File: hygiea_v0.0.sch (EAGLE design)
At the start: 45 parts, among them U1 3.3V/150mA, U2 BNO055, U3 CRYSTAL_8X3.8SMD

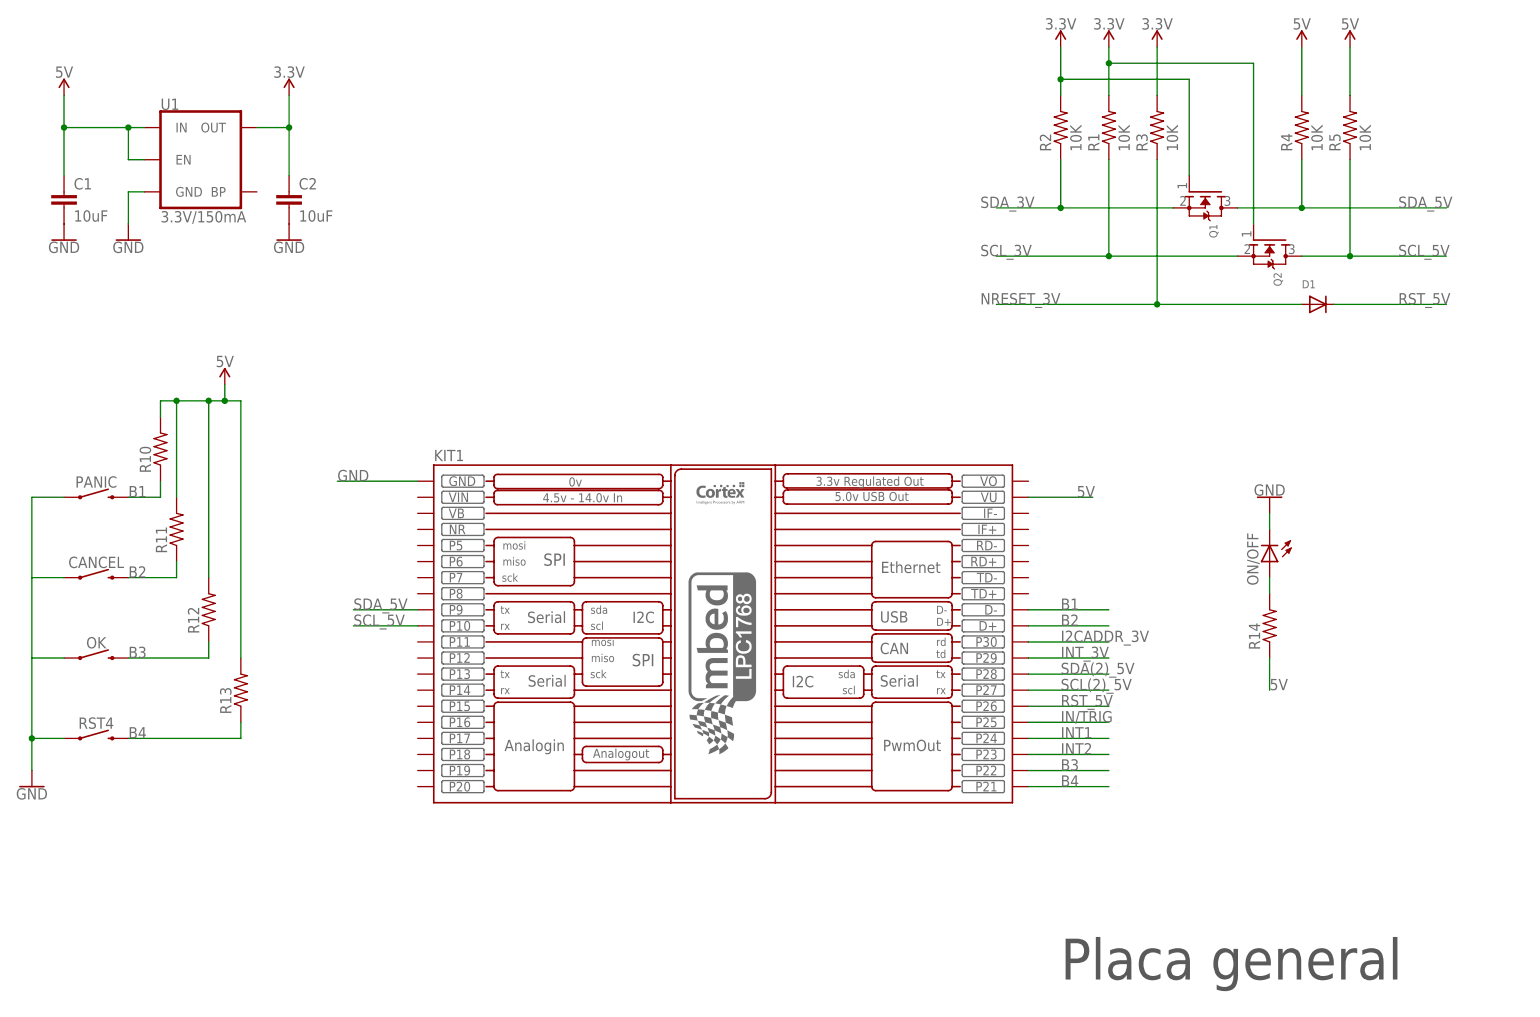
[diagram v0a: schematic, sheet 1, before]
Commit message: Version barata, push buttons standar
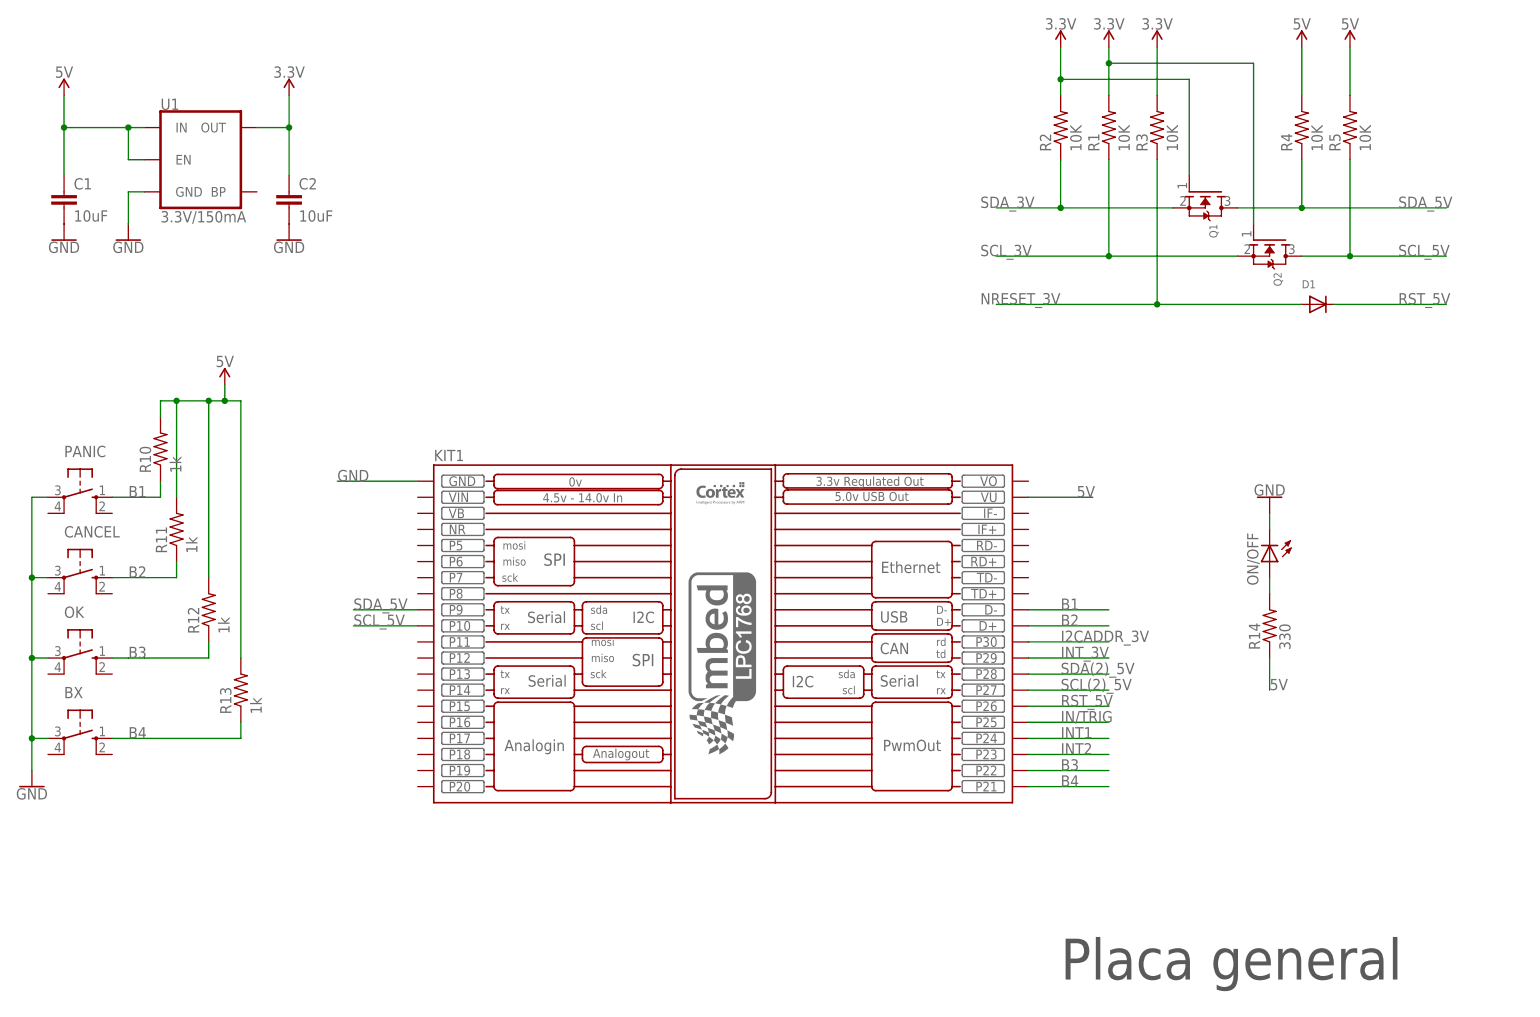
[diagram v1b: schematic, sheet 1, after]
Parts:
- removed RST4: MOMENTARY-SWITCH-SPST-SMD-5.2-REDUNDANT, SparkFun-Switches:MOMENTARY-SWITCH-SPST-SMD-5.2-REDUNDANT
- added BX: (no value), switch-omron:10-XX
- CANCEL, OK, PANIC, RST: value MOMENTARY-SWITCH-SPST-SMD-5.2-REDUNDANT -> (none); device SparkFun-Switches:MOMENTARY-SWITCH-SPST-SMD-5.2-REDUNDANT -> switch-omron:10-XX
- R10, R11, R12, R13: value (none) -> 1k
- R14: value (none) -> 330
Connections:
- net AT_RESET: now also RST.S; no longer RST.2
- net B1: now also PANIC.S; no longer PANIC.2
- net B2: now also CANCEL.S; no longer CANCEL.2
- net B3: now also OK.S; no longer OK.2
- net B4: now also BX.S; no longer RST4.2
- net GND: now also BX.P, CANCEL.P, OK.P, PANIC.P, RST.P; no longer CANCEL.1, OK.1, PANIC.1, RST.1, RST4.1
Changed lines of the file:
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@@
 <part name="GND19" library="SparkFun-PowerSymbols" deviceset="GND" device=""/>
 <part name="BLE/ICSP" library="adafruit" deviceset="PINHD-1X10" device=""/>
-<part name="RST" library="SparkFun-Switches" deviceset="MOMENTARY-SWITCH-SPST" device="-SMD-5.2-REDUNDANT" value=""/>
 <part name="R7" library="adafruit" deviceset="R-US_" device="R0805" value="1k"/>
 <part name="R8" library="adafruit" deviceset="R-US_" device="R0805" value="10k"/>
@@
 <part name="SUPPLY14" library="SparkFun-PowerSymbols" deviceset="5V" device=""/>
 <part name="JP1" library="jumper" library_urn="urn:adsk.eagle:library:252" deviceset="JP2E" device="" package3d_urn="urn:adsk.eagle:package:15452/1"/>
-<part name="PANIC" library="SparkFun-Switches" deviceset="MOMENTARY-SWITCH-SPST" device="-SMD-5.2-REDUNDANT" value=""/>
-<part name="CANCEL" library="SparkFun-Switches" deviceset="MOMENTARY-SWITCH-SPST" device="-SMD-5.2-REDUNDANT" value=""/>
-<part name="OK" library="SparkFun-Switches" deviceset="MOMENTARY-SWITCH-SPST" device="-SMD-5.2-REDUNDANT" value=""/>
-<part name="RST4" library="SparkFun-Switches" deviceset="MOMENTARY-SWITCH-SPST" device="-SMD-5.2-REDUNDANT" value=""/>
-<part name="R10" library="adafruit" deviceset="R-US_" device="R0805"/>
-<part name="R11" library="adafruit" deviceset="R-US_" device="R0805"/>
-<part name="R12" library="adafruit" deviceset="R-US_" device="R0805"/>
-<part name="R13" library="adafruit" deviceset="R-US_" device="R0805"/>
+<part name="R10" library="adafruit" deviceset="R-US_" device="R0805" value="1k"/>
+<part name="R11" library="adafruit" deviceset="R-US_" device="R0805" value="1k"/>
+<part name="R12" library="adafruit" deviceset="R-US_" device="R0805" value="1k"/>
+<part name="R13" library="adafruit" deviceset="R-US_" device="R0805" value="1k"/>
 <part name="GND22" library="SparkFun-PowerSymbols" deviceset="GND" device=""/>
 <part name="SUPPLY18" library="SparkFun-PowerSymbols" deviceset="5V" device=""/>
 <part name="ON/OFF" library="adafruit" deviceset="LED" device="CHIP-LED0805"/>
-<part name="R14" library="adafruit" deviceset="R-US_" device="R0805"/>
+<part name="R14" library="adafruit" deviceset="R-US_" device="R0805" value="330"/>
 <part name="GND23" library="SparkFun-PowerSymbols" deviceset="GND" device=""/>
+<part name="PANIC" library="switch-omron" library_urn="urn:adsk.eagle:library:377" deviceset="10-XX" device="" package3d_urn="urn:adsk.eagle:package:27496/1"/>
+<part name="CANCEL" library="switch-omron" library_urn="urn:adsk.eagle:library:377" deviceset="10-XX" device="" package3d_urn="urn:adsk.eagle:package:27496/1"/>
+<part name="OK" library="switch-omron" library_urn="urn:adsk.eagle:library:377" deviceset="10-XX" device="" package3d_urn="urn:adsk.eagle:package:27496/1"/>
+<part name="BX" library="switch-omron" library_urn="urn:adsk.eagle:library:377" deviceset="10-XX" device="" package3d_urn="urn:adsk.eagle:package:27496/1"/>
+<part name="RST" library="switch-omron" library_urn="urn:adsk.eagle:library:377" deviceset="10-XX" device="" package3d_urn="urn:adsk.eagle:package:27496/1"/>
 </parts>
 <sheets>
@@
 <instance part="SUPPLY4" gate="G$1" x="213.36" y="172.72"/>
 <instance part="SUPPLY5" gate="G$1" x="220.98" y="172.72"/>
-<instance part="PANIC" gate="G$1" x="22.86" y="101.6"/>
-<instance part="CANCEL" gate="G$1" x="22.86" y="88.9"/>
-<instance part="OK" gate="G$1" x="22.86" y="76.2"/>
-<instance part="RST4" gate="G$1" x="22.86" y="63.5"/>
 <instance part="R10" gate="G$1" x="33.02" y="109.22" rot="R90"/>
 <instance part="R11" gate="G$1" x="35.56" y="96.52" rot="R90"/>
@@
 <instance part="R14" gate="G$1" x="208.28" y="81.28" rot="R90"/>
 <instance part="GND23" gate="1" x="208.28" y="101.6" rot="R180"/>
+<instance part="PANIC" gate="1" x="20.32" y="101.6" rot="R270"/>
+<instance part="CANCEL" gate="1" x="20.32" y="88.9" rot="R270"/>
+<instance part="OK" gate="1" x="20.32" y="76.2" rot="R270"/>
+<instance part="BX" gate="1" x="20.32" y="63.5" rot="R270"/>
 </instances>
 <busses>
@@
 </segment>
 <segment>
-<pinref part="RST4" gate="G$1" pin="1"/>
 <pinref part="GND22" gate="1" pin="GND"/>
-<wire x1="17.78" y1="63.5" x2="12.7" y2="63.5" width="0.1524" layer="91"/>
+<pinref part="PANIC" gate="1" pin="P"/>
+<wire x1="15.24" y1="101.6" x2="12.7" y2="101.6" width="0.1524" layer="91"/>
+<wire x1="12.7" y1="101.6" x2="12.7" y2="88.9" width="0.1524" layer="91"/>
+<pinref part="CANCEL" gate="1" pin="P"/>
+<wire x1="12.7" y1="88.9" x2="12.7" y2="76.2" width="0.1524" layer="91"/>
+<wire x1="12.7" y1="76.2" x2="12.7" y2="63.5" width="0.1524" layer="91"/>
 <wire x1="12.7" y1="63.5" x2="12.7" y2="58.42" width="0.1524" layer="91"/>
-<pinref part="OK" gate="G$1" pin="1"/>
-<wire x1="17.78" y1="76.2" x2="12.7" y2="76.2" width="0.1524" layer="91"/>
+<wire x1="15.24" y1="88.9" x2="12.7" y2="88.9" width="0.1524" layer="91"/>
+<junction x="12.7" y="88.9"/>
+<pinref part="OK" gate="1" pin="P"/>
+<wire x1="15.24" y1="76.2" x2="12.7" y2="76.2" width="0.1524" layer="91"/>
+<junction x="12.7" y="76.2"/>
+<pinref part="BX" gate="1" pin="P"/>
+<wire x1="15.24" y1="63.5" x2="12.7" y2="63.5" width="0.1524" layer="91"/>
 <junction x="12.7" y="63.5"/>
-<pinref part="CANCEL" gate="G$1" pin="1"/>
-<wire x1="12.7" y1="76.2" x2="12.7" y2="63.5" width="0.1524" layer="91"/>
-<wire x1="17.78" y1="88.9" x2="12.7" y2="88.9" width="0.1524" layer="91"/>
-<pinref part="PANIC" gate="G$1" pin="1"/>
-<wire x1="12.7" y1="88.9" x2="12.7" y2="76.2" width="0.1524" layer="91"/>
-<wire x1="17.78" y1="101.6" x2="12.7" y2="101.6" width="0.1524" layer="91"/>
-<wire x1="12.7" y1="101.6" x2="12.7" y2="88.9" width="0.1524" layer="91"/>
 </segment>
 <segment>
@@
 <net name="B4" class="0">
 <segment>
-<pinref part="RST4" gate="G$1" pin="2"/>
 <pinref part="R13" gate="G$1" pin="1"/>
-<wire x1="27.94" y1="63.5" x2="45.72" y2="63.5" width="0.1524" layer="91"/>
+<wire x1="25.4" y1="63.5" x2="45.72" y2="63.5" width="0.1524" layer="91"/>
 <wire x1="45.72" y1="63.5" x2="45.72" y2="66.04" width="0.1524" layer="91"/>
 <label x="27.94" y="63.5" size="1.778" layer="95"/>
+<pinref part="BX" gate="1" pin="S"/>
 </segment>
 <segment>
@@
 <net name="B3" class="0">
 <segment>
-<pinref part="OK" gate="G$1" pin="2"/>
 <pinref part="R12" gate="G$1" pin="1"/>
-<wire x1="27.94" y1="76.2" x2="40.64" y2="76.2" width="0.1524" layer="91"/>
+<wire x1="27.94" y1="76.2" x2="30.48" y2="76.2" width="0.1524" layer="91"/>
+<wire x1="30.48" y1="76.2" x2="40.64" y2="76.2" width="0.1524" layer="91"/>
 <wire x1="40.64" y1="76.2" x2="40.64" y2="78.74" width="0.1524" layer="91"/>
 <label x="27.94" y="76.2" size="1.778" layer="95"/>
+<pinref part="OK" gate="1" pin="S"/>
+<wire x1="25.4" y1="76.2" x2="27.94" y2="76.2" width="0.1524" layer="91"/>
 </segment>
 <segment>
@@
 <net name="B2" class="0">
 <segment>
-<pinref part="CANCEL" gate="G$1" pin="2"/>
 <pinref part="R11" gate="G$1" pin="1"/>
-<wire x1="27.94" y1="88.9" x2="35.56" y2="88.9" width="0.1524" layer="91"/>
+<wire x1="25.4" y1="88.9" x2="35.56" y2="88.9" width="0.1524" layer="91"/>
 <wire x1="35.56" y1="88.9" x2="35.56" y2="91.44" width="0.1524" layer="91"/>
 <label x="27.94" y="88.9" size="1.778" layer="95"/>
+<pinref part="CANCEL" gate="1" pin="S"/>
 </segment>
 <segment>
@@
 <net name="B1" class="0">
 <segment>
-<pinref part="PANIC" gate="G$1" pin="2"/>
 <pinref part="R10" gate="G$1" pin="1"/>
-<wire x1="27.94" y1="101.6" x2="33.02" y2="101.6" width="0.1524" layer="91"/>
+<wire x1="25.4" y1="101.6" x2="33.02" y2="101.6" width="0.1524" layer="91"/>
 <wire x1="33.02" y1="101.6" x2="33.02" y2="104.14" width="0.1524" layer="91"/>
 <label x="27.94" y="101.6" size="1.778" layer="95"/>
+<pinref part="PANIC" gate="1" pin="S"/>
 </segment>
 <segment>
@@
 <instance part="FRAME4" gate="G$2" x="147.32" y="0"/>
 <instance part="AT-328P" gate="U1" x="132.08" y="88.9"/>
-<instance part="GND11" gate="1" x="35.56" y="123.444"/>
+<instance part="GND11" gate="1" x="35.56" y="103.124"/>
 <instance part="GND14" gate="1" x="104.394" y="55.88"/>
 <instance part="SUPPLY9" gate="G$1" x="53.34" y="157.48"/>
@@
 <instance part="GND19" gate="1" x="78.74" y="91.44" rot="R270"/>
 <instance part="BLE/ICSP" gate="G$1" x="218.44" y="121.92"/>
-<instance part="RST" gate="G$1" x="43.18" y="129.54"/>
 <instance part="R7" gate="G$1" x="53.34" y="149.86" rot="R90"/>
 <instance part="R8" gate="G$1" x="170.18" y="121.92" rot="R90"/>
@@
 <instance part="SUPPLY13" gate="G$1" x="170.18" y="129.54"/>
 <instance part="SUPPLY14" gate="G$1" x="177.8" y="129.54"/>
+<instance part="RST" gate="1" x="45.72" y="114.3" rot="R270"/>
 </instances>
 <busses>
@@
 </segment>
 <segment>
-<pinref part="RST" gate="G$1" pin="1"/>
-<wire x1="38.1" y1="129.54" x2="35.56" y2="129.54" width="0.1524" layer="91"/>
 <pinref part="GND11" gate="1" pin="GND"/>
-<wire x1="35.56" y1="129.54" x2="35.56" y2="125.984" width="0.1524" layer="91"/>
+<pinref part="RST" gate="1" pin="P"/>
+<wire x1="35.56" y1="114.3" x2="35.56" y2="105.664" width="0.1524" layer="91"/>
+<wire x1="40.64" y1="114.3" x2="35.56" y2="114.3" width="0.1524" layer="91"/>
 </segment>
 </net>
@@
 </segment>
 <segment>
-<pinref part="RST" gate="G$1" pin="2"/>
 <pinref part="R7" gate="G$1" pin="1"/>
-<wire x1="48.26" y1="129.54" x2="53.34" y2="129.54" width="0.1524" layer="91"/>
-<wire x1="53.34" y1="129.54" x2="53.34" y2="144.78" width="0.1524" layer="91"/>
 <label x="53.34" y="132.08" size="1.778" layer="95" rot="R90"/>
+<pinref part="RST" gate="1" pin="S"/>
+<wire x1="50.8" y1="114.3" x2="53.34" y2="114.3" width="0.1524" layer="91"/>
+<wire x1="53.34" y1="114.3" x2="53.34" y2="144.78" width="0.1524" layer="91"/>
 </segment>
 </net>
@@
 </sheet>
 </sheets>
+<errors>
+</errors>
 </schematic>
 </drawing>
